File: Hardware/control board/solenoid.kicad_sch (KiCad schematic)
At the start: 7 parts, among them J11 Screw_Terminal_01x02, Q3 NMOS

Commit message: schematic formatted
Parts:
- removed Q3: NMOS, symbol Simulation_SPICE:NMOS
- added Q1: 2N7002, Package_TO_SOT_SMD_AKL:SOT-23, symbol PCM_Transistor_MOSFET_AKL:2N7002
- D6: footprint (none) -> LED_THT:LED_D3.0mm
- J11: footprint (none) -> TerminalBlock_Phoenix:TerminalBlock_Phoenix_MPT-0,5-2-2.54_1x02_P2.54mm_Horizontal
- R1, R2, R9: footprint (none) -> Resistor_SMD:R_0805_2012Metric
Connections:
- net GND: now also Q1.2 (S)
- net at D5.2 (A), J11.2 (Pin_2), R9.2: now also Q1.3 (D)
- net at R1.2, R2.1: now also Q1.1 (G)
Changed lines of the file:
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@@
     (stroke (width 0) (type default))
   )
-  (wire (pts (xy 107.95 99.06) (xy 114.935 99.06))
+  (wire (pts (xy 107.95 99.06) (xy 116.205 99.06))
     (stroke (width 0) (type default))
   )
@@
   )
   (wire (pts (xy 122.555 86.36) (xy 122.555 90.805))
+    (stroke (width 0) (type default))
+  )
+  (wire (pts (xy 116.205 99.06) (xy 116.205 100.33))
     (stroke (width 0) (type default))
   )
@@
     (effects (font (size 1.27 1.27)) (justify right))
   )
-  (symbol (lib_id "Simulation_SPICE:NMOS") (at 120.015 99.06 0) (unit 1)
-    (in_bom yes) (on_board yes) (dnp no) (fields_autoplaced)
-    (property "Reference" "Q3" (at 125.73 97.79 0)
-      (effects (font (size 1.27 1.27)) (justify left))
-    )
-    (property "Value" "NMOS" (at 125.73 100.33 0)
-      (effects (font (size 1.27 1.27)) (justify left))
-    )
-    (property "Footprint" "" (at 125.095 96.52 0)
-      (effects (font (size 1.27 1.27)) hide)
-    )
-    (property "Datasheet" "https://ngspice.sourceforge.io/docs/ngspice-manual.pdf" (at 120.015 111.76 0)
-      (effects (font (size 1.27 1.27)) hide)
-    )
-    (property "Sim.Device" "NMOS" (at 120.015 116.205 0)
-      (effects (font (size 1.27 1.27)) hide)
-    )
-    (property "Sim.Type" "VDMOS" (at 120.015 118.11 0)
-      (effects (font (size 1.27 1.27)) hide)
-    )
-    (property "Sim.Pins" "1=D 2=G 3=S" (at 120.015 114.3 0)
-      (effects (font (size 1.27 1.27)) hide)
-    )
-    (pin "1")
-    (pin "2")
-    (pin "3")
-    (instances
-      (project "solenoid"
-        (path "/b4ed5960-473e-41d7-9d87-eb439ed22219"
-          (reference "Q3") (unit 1)
-        )
-      )
-      (project "control board"
-        (path "/cf0863a8-7f64-449b-8eb4-3c06c871fb37"
-          (reference "Q3") (unit 1)
-        )
-        (path "/cf0863a8-7f64-449b-8eb4-3c06c871fb37/9fd0b45f-6f46-40af-ae0d-29c33b45e498"
-          (reference "Q1") (unit 1)
-        )
-        (path "/cf0863a8-7f64-449b-8eb4-3c06c871fb37/6163a064-c95f-47b6-9c17-0e18c391c233"
-          (reference "Q2") (unit 1)
-        )
-        (path "/cf0863a8-7f64-449b-8eb4-3c06c871fb37/f39ce93b-3626-4dde-a021-b00a2c8134c7"
-          (reference "Q3") (unit 1)
-        )
-      )
-    )
-  )
   (symbol (lib_id "Device:LED") (at 129.54 79.375 90) (unit 1)
     (in_bom yes) (on_board yes) (dnp no) (fields_autoplaced)
@@
       (effects (font (size 1.27 1.27)) (justify right))
     )
-    (property "Footprint" "" (at 129.54 79.375 0)
+    (property "Footprint" "LED_THT:LED_D3.0mm" (at 129.54 79.375 0)
       (effects (font (size 1.27 1.27)) hide)
     )
@@
         )
         (path "/cf0863a8-7f64-449b-8eb4-3c06c871fb37/9fd0b45f-6f46-40af-ae0d-29c33b45e498"
-          (reference "Green") (unit 1)
+          (reference "Green1") (unit 1)
         )
         (path "/cf0863a8-7f64-449b-8eb4-3c06c871fb37/6163a064-c95f-47b6-9c17-0e18c391c233"
@@
       (effects (font (size 1.27 1.27)) (justify left))
     )
-    (property "Footprint" "" (at 158.75 88.265 0)
+    (property "Footprint" "TerminalBlock_Phoenix:TerminalBlock_Phoenix_MPT-0,5-2-2.54_1x02_P2.54mm_Horizontal" (at 158.75 88.265 0)
       (effects (font (size 1.27 1.27)) hide)
     )
@@
       (effects (font (size 1.27 1.27)))
     )
-    (property "Footprint" "" (at 101.219 98.044 90)
+    (property "Footprint" "Resistor_SMD:R_0805_2012Metric" (at 101.219 98.044 90)
       (effects (font (size 1.27 1.27)) hide)
     )
@@
       (effects (font (size 1.27 1.27)) (justify left))
     )
-    (property "Footprint" "" (at 108.966 106.299 90)
+    (property "Footprint" "Resistor_SMD:R_0805_2012Metric" (at 108.966 106.299 90)
       (effects (font (size 1.27 1.27)) hide)
     )
@@
       (effects (font (size 1.27 1.27)) (justify left))
     )
-    (property "Footprint" "" (at 130.556 87.249 90)
+    (property "Footprint" "Resistor_SMD:R_0805_2012Metric" (at 130.556 87.249 90)
       (effects (font (size 1.27 1.27)) hide)
     )
@@
         )
       )
+    )
+  )
+  (symbol (lib_id "PCM_Transistor_MOSFET_AKL:2N7002") (at 120.015 99.06 0) (unit 1)
+    (in_bom yes) (on_board yes) (dnp no) (fields_autoplaced)
+    (property "Reference" "Q1" (at 126.365 97.79 0)
+      (effects (font (size 1.27 1.27)) (justify left))
+    )
+    (property "Value" "2N7002" (at 126.365 100.33 0)
+      (effects (font (size 1.27 1.27)) (justify left))
+    )
+    (property "Footprint" "Package_TO_SOT_SMD_AKL:SOT-23" (at 125.095 96.52 0)
+      (effects (font (size 1.27 1.27)) hide)
+    )
+    (property "Datasheet" "https://www.tme.eu/Document/7df5cae36abdfcedddb681f5be886f05/2N7000.pdf" (at 120.015 99.06 0)
+      (effects (font (size 1.27 1.27)) hide)
+    )
+    (pin "1")
+    (pin "2")
+    (pin "3")
+    (instances
+      (project "control board"
+        (path "/cf0863a8-7f64-449b-8eb4-3c06c871fb37/9fd0b45f-6f46-40af-ae0d-29c33b45e498"
+          (reference "Q1") (unit 1)
+        )
+        (path "/cf0863a8-7f64-449b-8eb4-3c06c871fb37/6163a064-c95f-47b6-9c17-0e18c391c233"
+          (reference "Q2") (unit 1)
+        )
+        (path "/cf0863a8-7f64-449b-8eb4-3c06c871fb37/f39ce93b-3626-4dde-a021-b00a2c8134c7"
+          (reference "Q3") (unit 1)
+        )
+      )

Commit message: Revert "Merge branch 'hardware' of https://github.com/bruin-underwater-robotics/2023-2024 into hardware"
This reverts commit f5050c74fbd2d727488e15b71bfb24c9149407df, reversing
changes made to d4ffa11f2369dfdbeb25d57bd1642de1ab50c466.
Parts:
- removed Q1: 2N7002, Package_TO_SOT_SMD_AKL:SOT-23, symbol PCM_Transistor_MOSFET_AKL:2N7002
- added Q3: NMOS, symbol Simulation_SPICE:NMOS
- D6: footprint LED_THT:LED_D3.0mm -> (none)
- J11: footprint TerminalBlock_Phoenix:TerminalBlock_Phoenix_MPT-0,5-2-2.54_1x02_P2.54mm_Horizontal -> (none)
- R1, R2, R9: footprint Resistor_SMD:R_0805_2012Metric -> (none)
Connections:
- net GND: now also Q3.3 (S)
- net at D5.2 (A), J11.2 (Pin_2), R9.2: now also Q3.1 (D)
- net at R1.2, R2.1: now also Q3.2 (G)
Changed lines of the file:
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@@
     (stroke (width 0) (type default))
   )
-  (wire (pts (xy 107.95 99.06) (xy 116.205 99.06))
+  (wire (pts (xy 107.95 99.06) (xy 114.935 99.06))
     (stroke (width 0) (type default))
   )
@@
   )
   (wire (pts (xy 122.555 86.36) (xy 122.555 90.805))
-    (stroke (width 0) (type default))
-  )
-  (wire (pts (xy 116.205 99.06) (xy 116.205 100.33))
     (stroke (width 0) (type default))
   )
@@
     (effects (font (size 1.27 1.27)) (justify right))
   )
+  (symbol (lib_id "Simulation_SPICE:NMOS") (at 120.015 99.06 0) (unit 1)
+    (in_bom yes) (on_board yes) (dnp no) (fields_autoplaced)
+    (property "Reference" "Q3" (at 125.73 97.79 0)
+      (effects (font (size 1.27 1.27)) (justify left))
+    )
+    (property "Value" "NMOS" (at 125.73 100.33 0)
+      (effects (font (size 1.27 1.27)) (justify left))
+    )
+    (property "Footprint" "" (at 125.095 96.52 0)
+      (effects (font (size 1.27 1.27)) hide)
+    )
+    (property "Datasheet" "https://ngspice.sourceforge.io/docs/ngspice-manual.pdf" (at 120.015 111.76 0)
+      (effects (font (size 1.27 1.27)) hide)
+    )
+    (property "Sim.Device" "NMOS" (at 120.015 116.205 0)
+      (effects (font (size 1.27 1.27)) hide)
+    )
+    (property "Sim.Type" "VDMOS" (at 120.015 118.11 0)
+      (effects (font (size 1.27 1.27)) hide)
+    )
+    (property "Sim.Pins" "1=D 2=G 3=S" (at 120.015 114.3 0)
+      (effects (font (size 1.27 1.27)) hide)
+    )
+    (pin "1")
+    (pin "2")
+    (pin "3")
+    (instances
+      (project "solenoid"
+        (path "/b4ed5960-473e-41d7-9d87-eb439ed22219"
+          (reference "Q3") (unit 1)
+        )
+      )
+      (project "control board"
+        (path "/cf0863a8-7f64-449b-8eb4-3c06c871fb37"
+          (reference "Q3") (unit 1)
+        )
+        (path "/cf0863a8-7f64-449b-8eb4-3c06c871fb37/9fd0b45f-6f46-40af-ae0d-29c33b45e498"
+          (reference "Q1") (unit 1)
+        )
+        (path "/cf0863a8-7f64-449b-8eb4-3c06c871fb37/6163a064-c95f-47b6-9c17-0e18c391c233"
+          (reference "Q2") (unit 1)
+        )
+        (path "/cf0863a8-7f64-449b-8eb4-3c06c871fb37/f39ce93b-3626-4dde-a021-b00a2c8134c7"
+          (reference "Q3") (unit 1)
+        )
+      )
+    )
+  )
   (symbol (lib_id "Device:LED") (at 129.54 79.375 90) (unit 1)
     (in_bom yes) (on_board yes) (dnp no) (fields_autoplaced)
@@
       (effects (font (size 1.27 1.27)) (justify right))
     )
-    (property "Footprint" "LED_THT:LED_D3.0mm" (at 129.54 79.375 0)
+    (property "Footprint" "" (at 129.54 79.375 0)
       (effects (font (size 1.27 1.27)) hide)
     )
@@
         )
         (path "/cf0863a8-7f64-449b-8eb4-3c06c871fb37/9fd0b45f-6f46-40af-ae0d-29c33b45e498"
-          (reference "Green1") (unit 1)
+          (reference "Green") (unit 1)
         )
         (path "/cf0863a8-7f64-449b-8eb4-3c06c871fb37/6163a064-c95f-47b6-9c17-0e18c391c233"
@@
       (effects (font (size 1.27 1.27)) (justify left))
     )
-    (property "Footprint" "TerminalBlock_Phoenix:TerminalBlock_Phoenix_MPT-0,5-2-2.54_1x02_P2.54mm_Horizontal" (at 158.75 88.265 0)
+    (property "Footprint" "" (at 158.75 88.265 0)
       (effects (font (size 1.27 1.27)) hide)
     )
@@
       (effects (font (size 1.27 1.27)))
     )
-    (property "Footprint" "Resistor_SMD:R_0805_2012Metric" (at 101.219 98.044 90)
+    (property "Footprint" "" (at 101.219 98.044 90)
       (effects (font (size 1.27 1.27)) hide)
     )
@@
       (effects (font (size 1.27 1.27)) (justify left))
     )
-    (property "Footprint" "Resistor_SMD:R_0805_2012Metric" (at 108.966 106.299 90)
+    (property "Footprint" "" (at 108.966 106.299 90)
       (effects (font (size 1.27 1.27)) hide)
     )
@@
       (effects (font (size 1.27 1.27)) (justify left))
     )
-    (property "Footprint" "Resistor_SMD:R_0805_2012Metric" (at 130.556 87.249 90)
+    (property "Footprint" "" (at 130.556 87.249 90)
       (effects (font (size 1.27 1.27)) hide)
     )
@@
         )
       )
-    )
-  )
-  (symbol (lib_id "PCM_Transistor_MOSFET_AKL:2N7002") (at 120.015 99.06 0) (unit 1)
-    (in_bom yes) (on_board yes) (dnp no) (fields_autoplaced)
-    (property "Reference" "Q1" (at 126.365 97.79 0)
-      (effects (font (size 1.27 1.27)) (justify left))
-    )
-    (property "Value" "2N7002" (at 126.365 100.33 0)
-      (effects (font (size 1.27 1.27)) (justify left))
-    )
-    (property "Footprint" "Package_TO_SOT_SMD_AKL:SOT-23" (at 125.095 96.52 0)
-      (effects (font (size 1.27 1.27)) hide)
-    )
-    (property "Datasheet" "https://www.tme.eu/Document/7df5cae36abdfcedddb681f5be886f05/2N7000.pdf" (at 120.015 99.06 0)
-      (effects (font (size 1.27 1.27)) hide)
-    )
-    (pin "1")
-    (pin "2")
-    (pin "3")
-    (instances
-      (project "control board"
-        (path "/cf0863a8-7f64-449b-8eb4-3c06c871fb37/9fd0b45f-6f46-40af-ae0d-29c33b45e498"
-          (reference "Q1") (unit 1)
-        )
-        (path "/cf0863a8-7f64-449b-8eb4-3c06c871fb37/6163a064-c95f-47b6-9c17-0e18c391c233"
-          (reference "Q2") (unit 1)
-        )
-        (path "/cf0863a8-7f64-449b-8eb4-3c06c871fb37/f39ce93b-3626-4dde-a021-b00a2c8134c7"
-          (reference "Q3") (unit 1)
-        )
-      )

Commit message: fixing stupid mistakes
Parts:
- D6: footprint (none) -> LED_THT:LED_D3.0mm
- J11: footprint (none) -> Library:TE_282836-2
- Q3: footprint (none) -> PCM_Package_TO_SOT_SMD_AKL:TSOT-23_BigPads
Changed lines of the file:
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@@
       (effects (font (size 1.27 1.27)) (justify left))
     )
-    (property "Footprint" "" (at 125.095 96.52 0)
+    (property "Footprint" "PCM_Package_TO_SOT_SMD_AKL:TSOT-23_BigPads" (at 125.095 96.52 0)
       (effects (font (size 1.27 1.27)) hide)
     )
@@
       (effects (font (size 1.27 1.27)) (justify right))
     )
-    (property "Footprint" "" (at 129.54 79.375 0)
+    (property "Footprint" "LED_THT:LED_D3.0mm" (at 129.54 79.375 0)
       (effects (font (size 1.27 1.27)) hide)
     )
@@
         )
         (path "/cf0863a8-7f64-449b-8eb4-3c06c871fb37/9fd0b45f-6f46-40af-ae0d-29c33b45e498"
-          (reference "Green") (unit 1)
+          (reference "Green1") (unit 1)
         )
         (path "/cf0863a8-7f64-449b-8eb4-3c06c871fb37/6163a064-c95f-47b6-9c17-0e18c391c233"
@@
       (effects (font (size 1.27 1.27)) (justify left))
     )
-    (property "Footprint" "" (at 158.75 88.265 0)
+    (property "Footprint" "Library:TE_282836-2" (at 158.75 88.265 0)
       (effects (font (size 1.27 1.27)) hide)
     )

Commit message: footprint work
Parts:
- R1, R2, R9: footprint (none) -> Resistor_SMD:R_0805_2012Metric
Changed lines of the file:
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@@
       (effects (font (size 1.27 1.27)))
     )
-    (property "Footprint" "" (at 101.219 98.044 90)
+    (property "Footprint" "Resistor_SMD:R_0805_2012Metric" (at 101.219 98.044 90)
       (effects (font (size 1.27 1.27)) hide)
     )
@@
       (effects (font (size 1.27 1.27)) (justify left))
     )
-    (property "Footprint" "" (at 108.966 106.299 90)
+    (property "Footprint" "Resistor_SMD:R_0805_2012Metric" (at 108.966 106.299 90)
       (effects (font (size 1.27 1.27)) hide)
     )
@@
       (effects (font (size 1.27 1.27)) (justify left))
     )
-    (property "Footprint" "" (at 130.556 87.249 90)
+    (property "Footprint" "Resistor_SMD:R_0805_2012Metric" (at 130.556 87.249 90)
       (effects (font (size 1.27 1.27)) hide)
     )

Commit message: control board clean up
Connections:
- net +14.8V: now also J11.2 (Pin_2); no longer J11.1 (Pin_1)
- net at D5.2 (A), Q3.1 (D), R9.2: now also J11.1 (Pin_1); no longer J11.2 (Pin_2)
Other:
- moved on the sheet: D5, D6, J11, Q3, R1, R2, R9

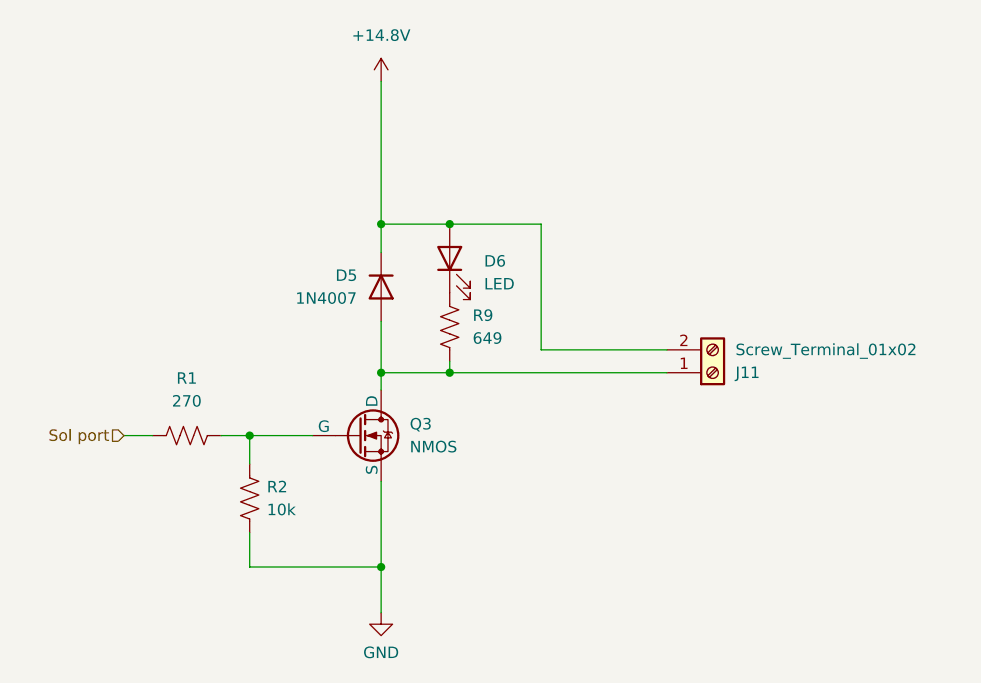
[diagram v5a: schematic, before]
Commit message: Update solenoid.kicad_sch
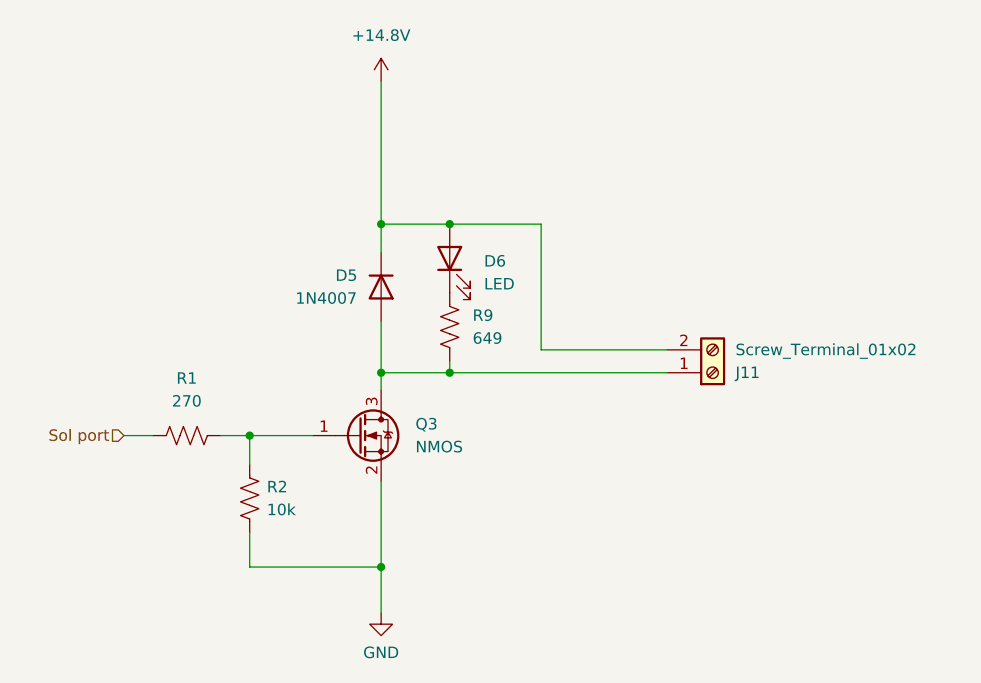
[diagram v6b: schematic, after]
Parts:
- Q3: footprint PCM_Package_TO_SOT_SMD_AKL:TSOT-23_BigPads -> Package_TO_SOT_SMD:SOT-23; symbol Simulation_SPICE:NMOS -> Transistor_FET:2N7002
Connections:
- net GND: now also Q3.2 (S); no longer Q3.3 (S)
- net at D5.2 (A), J11.1 (Pin_1), R9.2: now also Q3.3 (D); no longer Q3.1 (D)
- net at R1.2, R2.1: now also Q3.1 (G); no longer Q3.2 (G)
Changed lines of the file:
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@@
     (effects (font (size 1.27 1.27)) (justify right))
   )
-  (symbol (lib_id "Simulation_SPICE:NMOS") (at 119.38 99.695 0) (unit 1)
+  (symbol (lib_id "Transistor_FET:2N7002") (at 119.38 99.695 0) (unit 1)
     (in_bom yes) (on_board yes) (dnp no) (fields_autoplaced)
-    (property "Reference" "Q3" (at 125.095 98.425 0)
+    (property "Reference" "Q3" (at 125.73 98.425 0)
       (effects (font (size 1.27 1.27)) (justify left))
     )
-    (property "Value" "NMOS" (at 125.095 100.965 0)
+    (property "Value" "NMOS" (at 125.73 100.965 0)
       (effects (font (size 1.27 1.27)) (justify left))
     )
-    (property "Footprint" "PCM_Package_TO_SOT_SMD_AKL:TSOT-23_BigPads" (at 124.46 97.155 0)
-      (effects (font (size 1.27 1.27)) hide)
+    (property "Footprint" "Package_TO_SOT_SMD:SOT-23" (at 124.46 101.6 0)
+      (effects (font (size 1.27 1.27) italic) (justify left) hide)
     )
-    (property "Datasheet" "https://ngspice.sourceforge.io/docs/ngspice-manual.pdf" (at 119.38 112.395 0)
-      (effects (font (size 1.27 1.27)) hide)
+    (property "Datasheet" "https://www.onsemi.com/pub/Collateral/NDS7002A-D.PDF" (at 119.38 99.695 0)
+      (effects (font (size 1.27 1.27)) (justify left) hide)
     )
     (property "Sim.Device" "NMOS" (at 119.38 116.84 0)
